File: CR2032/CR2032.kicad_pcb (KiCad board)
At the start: 2 copper layers, 33 x 26 mm, 8 parts, among them J1 Conn_01x06

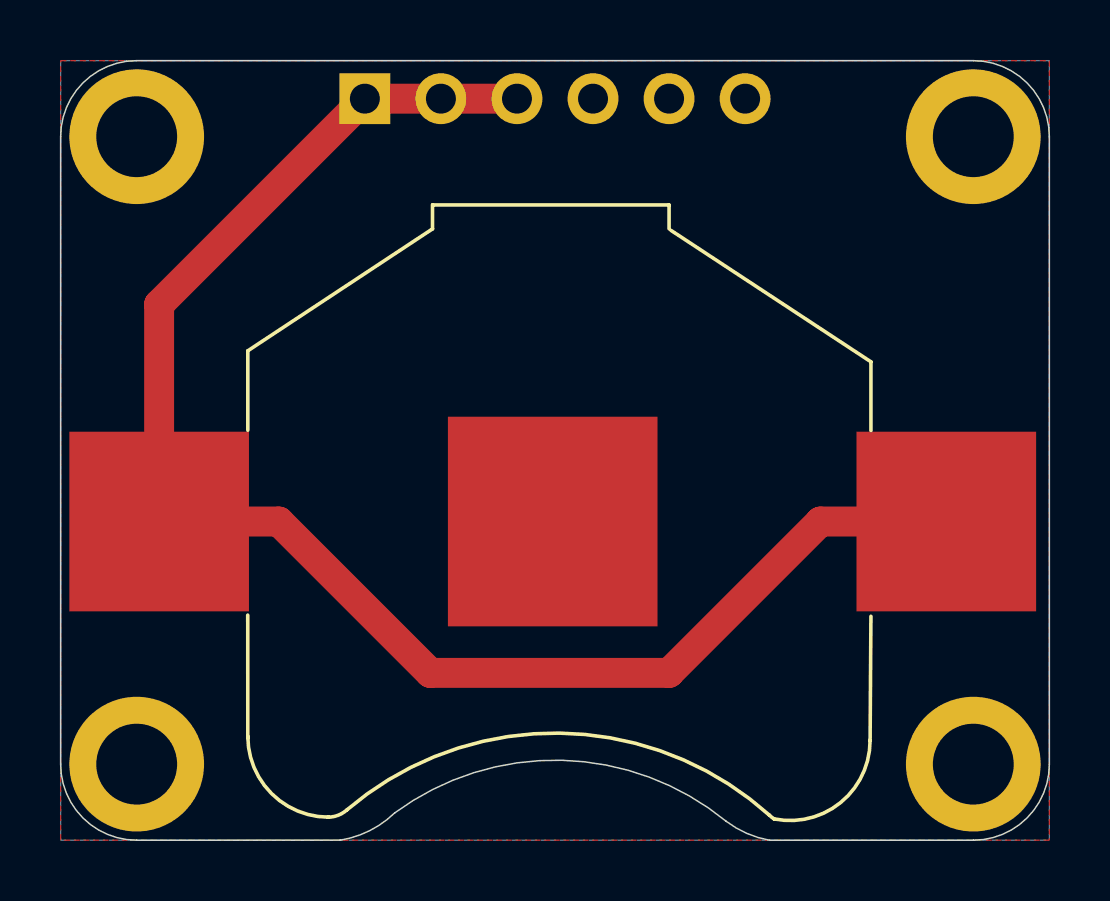
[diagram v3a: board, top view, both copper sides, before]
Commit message: Board size updated
Board size changed from 33.02mmX26.035mm to 33.02mmX25.4mm
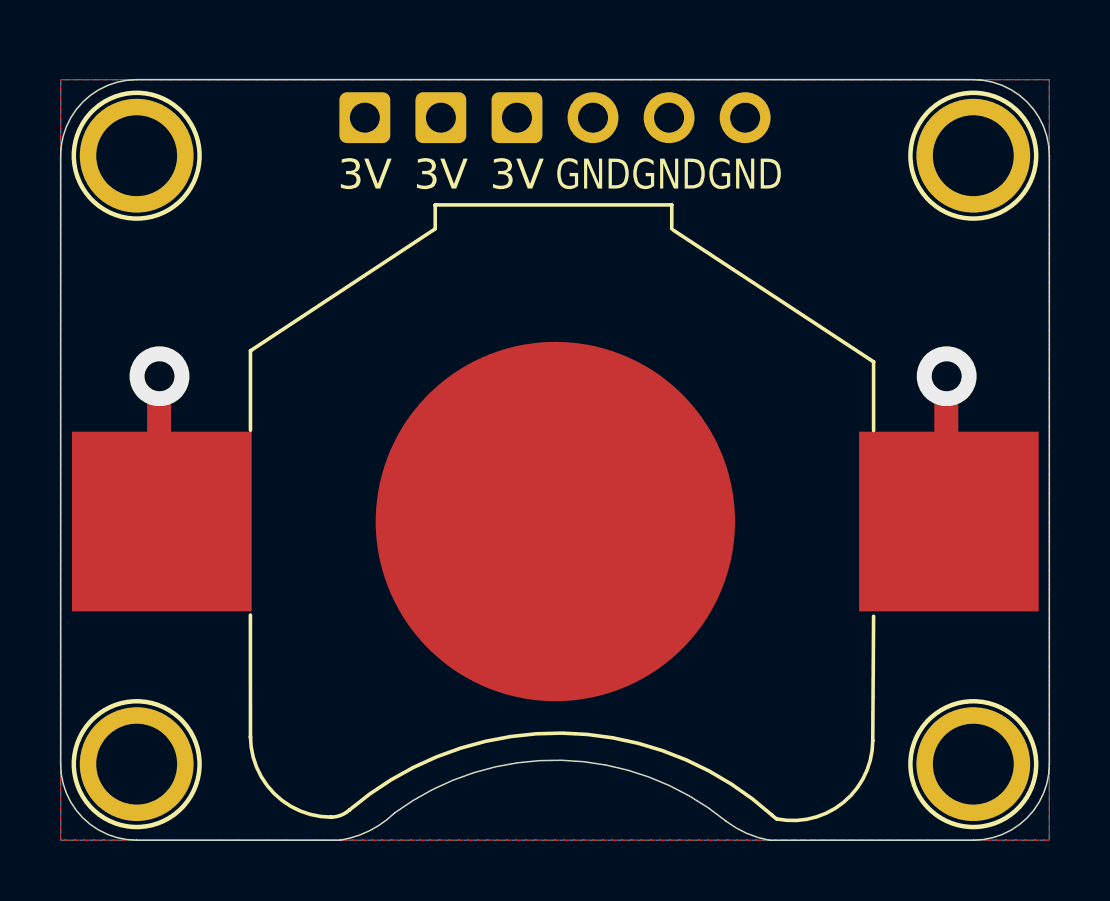
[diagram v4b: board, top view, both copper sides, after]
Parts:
- H1, H2, H3, H4: footprint MountingHole:MountingHole_2.7mm_M2.5_ISO14580_Pad -> SirBoardLibrary:MountingHole_M2.5_SirBoard
- moved H1 27.9 mm to (51.9, 30.4)
- moved H3 27.9 mm to (79.9, 30.4)
- moved H2 27.9 mm to (51.9, 50.7)
- moved H4 27.9 mm to (79.9, 50.7)
- moved J1 0.63 mm to (59.6, 29.1)
- moved BT1 0.09 mm to (66.0, 42.4)
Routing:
- net +3V0: track 52.5 -> 9.71 mm, vias 0 -> 2
- added copper zone on B.Cu, net +3V0
- removed copper zone on B.Cu, net GND
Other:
- board size 33 x 26 mm -> 33 x 25.4 mm
- board text added: "3V"
- board text added: "GND"

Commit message: Breakout Boards Revision 2
Renders updated, silkscreen text improved, blurry silkscreen items removed/resized.
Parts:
- G***: footprint logo:SirBoard140x44 -> logo:SirBoard171x54
